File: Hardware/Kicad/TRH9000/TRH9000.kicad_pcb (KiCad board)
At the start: 2 copper layers, 99.1 x 63.5 mm, 63 parts, among them J1 RGB, J100 MSX_SLOT_CONNECTOR, J2 S-Video, J3 Composite, Q1 BC817, U1 V9990, U2 KM428C256, U3 KM428C256, U4 74HC138, U5 74HC32, U6 CXA2075M, X1 14.318Mhz, Y1 21.47727Mhz

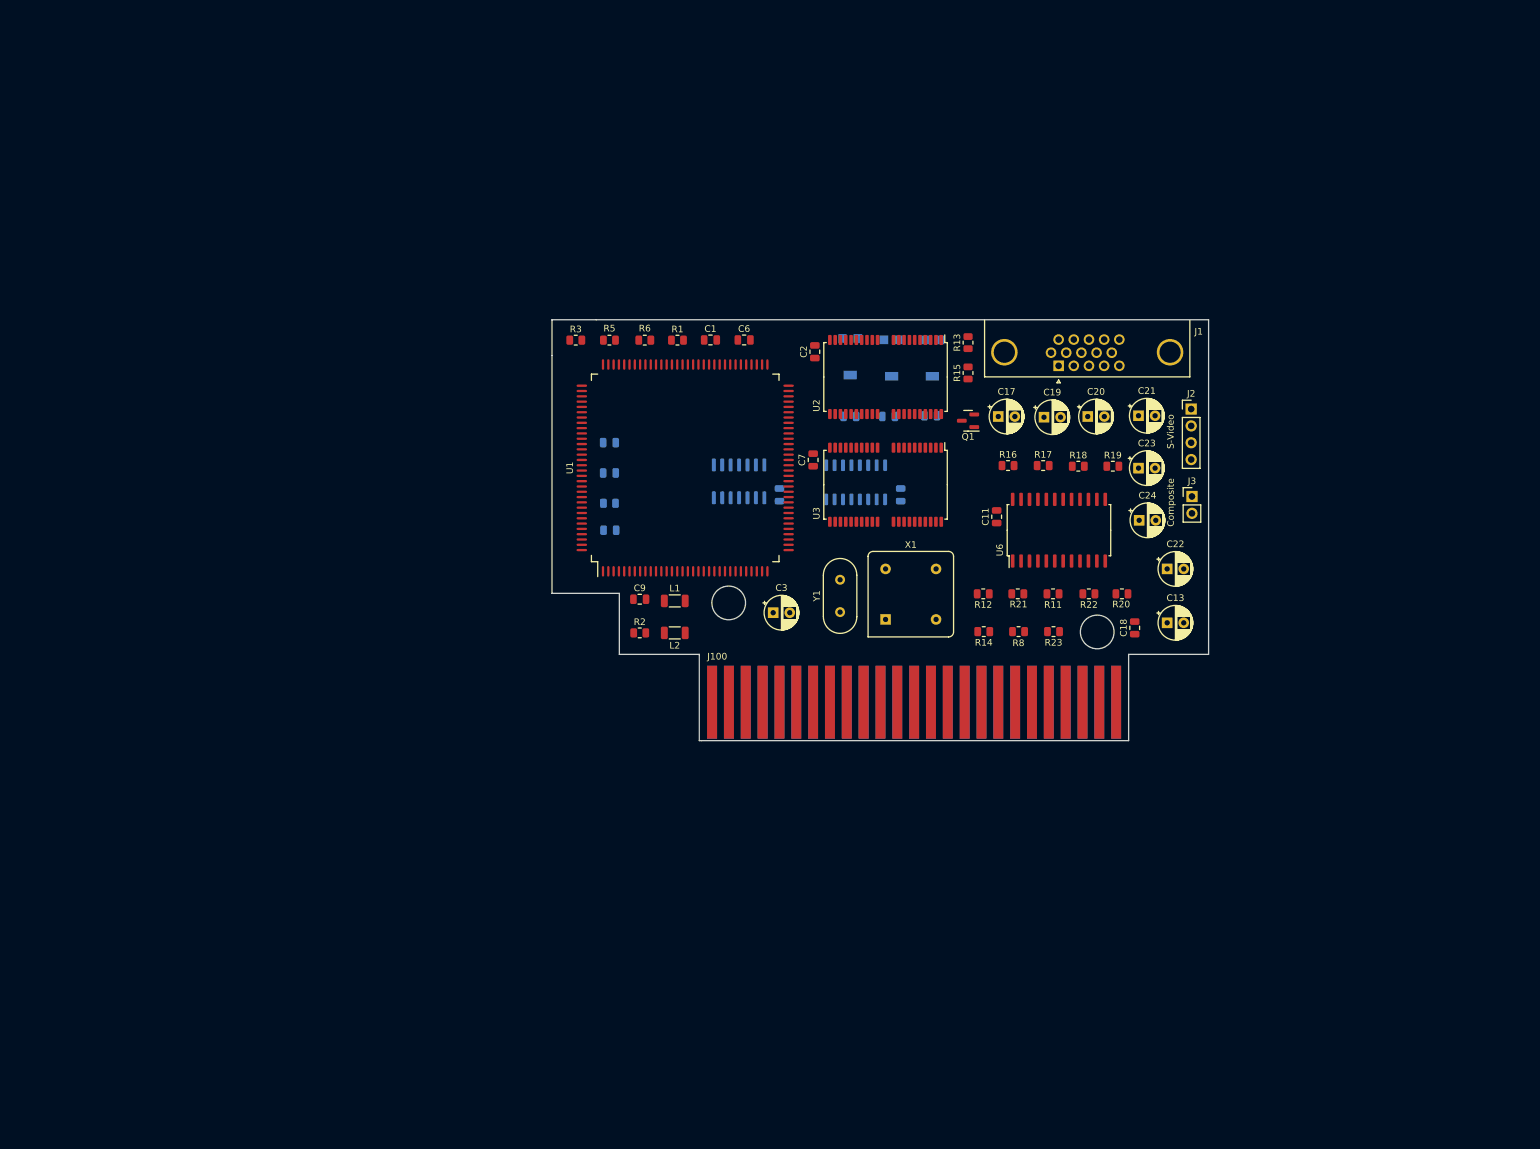
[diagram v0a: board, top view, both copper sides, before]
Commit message: Routing 1. First 3d view of the current PCB.
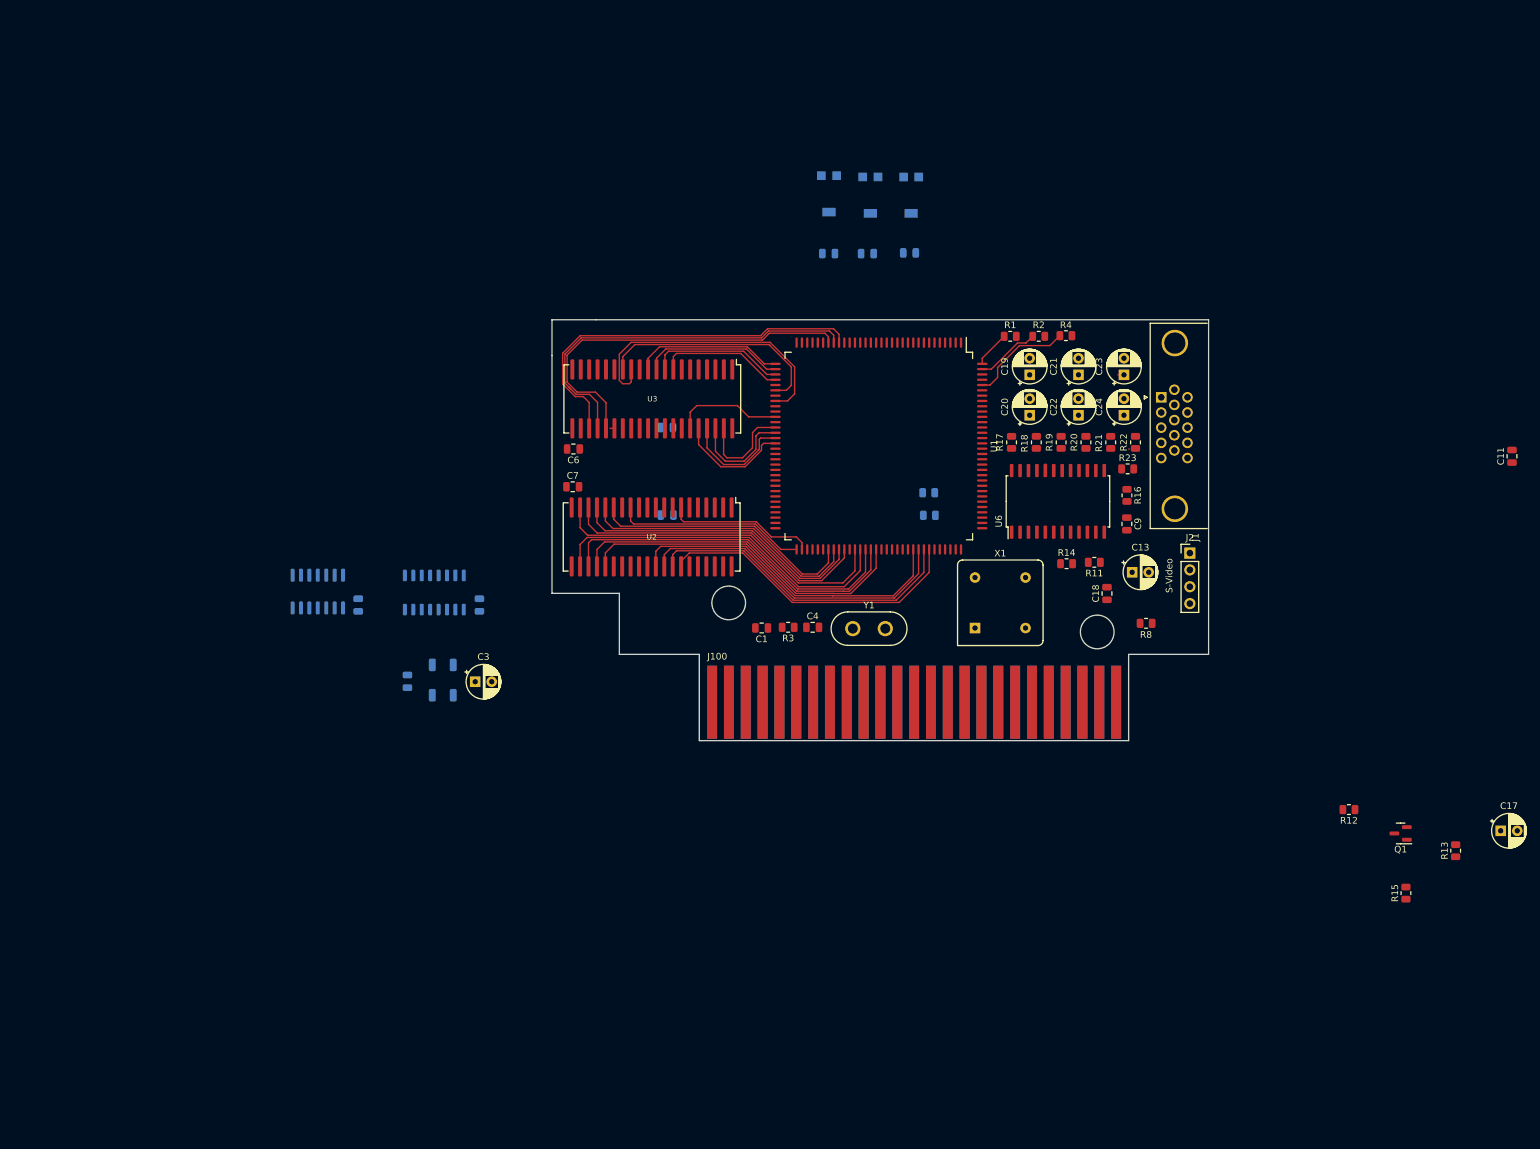
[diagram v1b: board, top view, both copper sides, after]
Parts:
- removed J3: Composite, Connector_PinHeader_2.54mm:PinHeader_1x02_P2.54mm_Vertical
- C2, L1, L2, R5, R6: moved to B.Cu
- C4, R4: moved to F.Cu
- U2, U3: footprint trh9000:TSOP-II-40_10.16x18.41mm_P0.8mm -> trh9000:SOJ-40_400mil
- Y1: footprint Crystal:Crystal_HC49-U_Vertical -> Crystal:Crystal_HC50_Vertical
- moved R13 106.2 mm to (234.6, 143.6)
- moved R15 102.6 mm to (227.1, 150.0)
- moved C17 98.2 mm to (241.4, 140.6)
- moved Q1 90.2 mm to (226.3, 141.0)
- moved C2 79.1 mm to (76.5, 118.0)
- moved C11 78.3 mm to (243.1, 84.1)
- moved R2 75.0 mm to (171.7, 66.0), turned to 180 degrees
- moved C9 74.4 mm to (185.0, 94.3), turned to -90 degrees
- moved R4 73.4 mm to (175.8, 65.9)
- moved C10 65.7 mm to (87.3, 106.5)
- moved U5 65.7 mm to (62.9, 104.5)
- moved C12 65.7 mm to (69.0, 106.5)
- moved U4 65.7 mm to (80.5, 104.6)
- moved R12 64.1 mm to (218.5, 137.4)
- moved R3 53.9 mm to (133.9, 109.9), turned to 180 degrees
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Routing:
- net /VDP/V0A2: track 0.00 -> 58.5 mm
- net /VDP/V0A1: track 0.00 -> 58.1 mm
- net /VDP/V0A0: track 0.00 -> 57.0 mm
- net /VDP/V1A3: track 0.00 -> 53.3 mm
- net /VDP/V1A2: track 0.00 -> 53.1 mm
- net /VDP/V1A4: track 0.00 -> 52.0 mm
- net /VDP/V1A1: track 0.00 -> 51.9 mm
- net /VDP/V1A0: track 0.00 -> 50.9 mm
- net /VDP/V1D4: track 0.00 -> 49.7 mm
- net /VDP/V1D5: track 0.00 -> 48.8 mm
- net /VDP/V1D6: track 0.00 -> 48.2 mm
- net /VDP/V1A5: track 0.00 -> 47.4 mm
- net /VDP/V1D7: track 0.00 -> 47.2 mm
- net /VDP/V1A6: track 0.00 -> 45.0 mm
- net Net-(U1-Pad40): track 0.00 -> 44.1 mm
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
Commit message: Many changes, among them, replacing the Composite out with SCART-rgb.
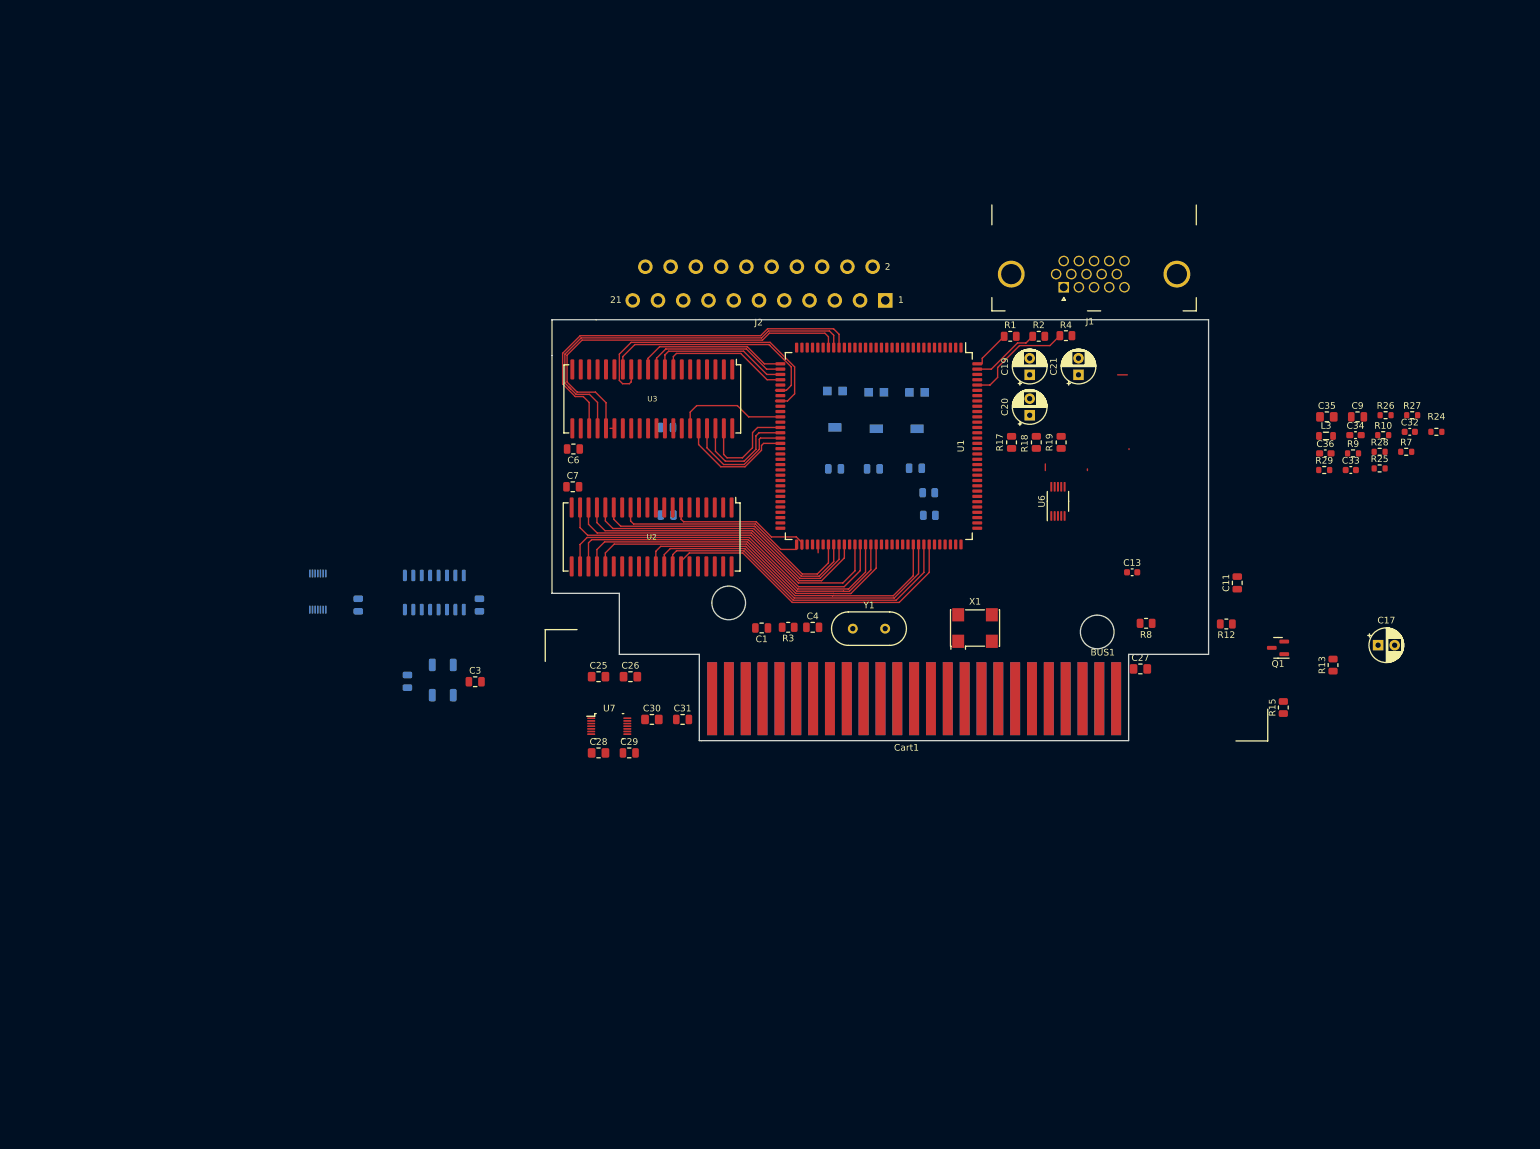
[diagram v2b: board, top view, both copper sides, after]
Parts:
- removed C18: 47pF, Capacitor_SMD:C_0805_2012Metric
- removed C22, C23, C24: 220uF, Capacitor_THT:CP_Radial_D5.0mm_P2.50mm
- removed J100: MSX_SLOT_CONNECTOR, msx:msx_cartridge
- removed R11: 4K7, Resistor_SMD:R_0805_2012Metric
- removed R14: 2K2, Resistor_SMD:R_0805_2012Metric
- removed R16: 2K61, Resistor_SMD:R_0805_2012Metric
- removed R20: 43R, Resistor_SMD:R_0805_2012Metric
- removed R21, R22: 75R, Resistor_SMD:R_0805_2012Metric
- removed R23: 240R, Resistor_SMD:R_0805_2012Metric
- removed REF**: OSHW-Logo_11.4x12mm_SilkScreen, Symbol:OSHW-Logo_11.4x12mm_SilkScreen
- added BUS1: MSX_SLOT_EDGE-CON, trh9000:msx_cartridge, F.Cu at (152.9, 120.8)
- added C25: C_CL21B105KBFNNNF, Capacitor_SMD:C_0805_2012Metric_Pad1.18x1.45mm_HandSolder, F.Cu at (105.3, 117.3)
- added C26: C_CL21B105KBFNNNF, Capacitor_SMD:C_0805_2012Metric_Pad1.18x1.45mm_HandSolder, F.Cu at (110.1, 117.3)
- added C27: C_CL21B105KBFNNNF, Capacitor_SMD:C_0805_2012Metric_Pad1.18x1.45mm_HandSolder, F.Cu at (187.0, 116.2)
- added C28: C_CL21B105KBFNNNF, Capacitor_SMD:C_0805_2012Metric_Pad1.18x1.45mm_HandSolder, F.Cu at (105.3, 128.8)
- added C29: C_CC0805JPX7R9BB104, Capacitor_SMD:C_0805_2012Metric, F.Cu at (109.9, 128.8)
- added C30: C_CL21B105KBFNNNF, Capacitor_SMD:C_0805_2012Metric_Pad1.18x1.45mm_HandSolder, F.Cu at (113.3, 123.8)
- added C31: C_CC0805JPX7R9BB104, Capacitor_SMD:C_0805_2012Metric, F.Cu at (118.0, 123.8)
- added C32: 47pF, Capacitor_SMD:C_0603_1608Metric, F.Cu at (227.7, 80.4)
- added C33: 47pF, Capacitor_SMD:C_0603_1608Metric, F.Cu at (218.8, 86.2)
- added C34: C_CL10B104KB8NNNL, Capacitor_SMD:C_0603_1608Metric_Pad1.08x0.95mm_HandSolder, F.Cu at (219.5, 80.9)
- added C35: C_GRM21BR71A106KA73K, Capacitor_SMD:C_0805_2012Metric_Pad1.18x1.45mm_HandSolder, F.Cu at (215.2, 78.2)
- added C36: C_CL10B104KB8NNNL, Capacitor_SMD:C_0603_1608Metric_Pad1.08x0.95mm_HandSolder, F.Cu at (214.9, 83.7)
- added Cart1: MSX-cartridge_dummy, trh9000:MSX-cart-dummy, F.Cu at (151.8, 118.7)
- added L3: L_MLZ2012M4R7HT000, Inductor_SMD:L_0805_2012Metric, F.Cu at (215.0, 81.0)
- added R10: 100, Resistor_SMD:R_0603_1608Metric, F.Cu at (223.7, 80.9)
- added R24: R_RC0603FR-0710KL, LRJ:R_0603_1608Metric_roundcourt, F.Cu at (231.7, 80.4)
- added R25: 100, Resistor_SMD:R_0603_1608Metric, F.Cu at (223.1, 85.9)
- added R26: 100, Resistor_SMD:R_0603_1608Metric, F.Cu at (224.0, 77.9)
- added R27: 100, Resistor_SMD:R_0603_1608Metric, F.Cu at (228.0, 77.9)
- added R28: 100, Resistor_SMD:R_0603_1608Metric, F.Cu at (223.1, 83.4)
- added R29: 1k, Resistor_SMD:R_0603_1608Metric, F.Cu at (214.8, 86.2)
- added R7: R_ERJ-3GEYJ105V, Resistor_SMD:R_0603_1608Metric, F.Cu at (227.1, 83.4)
- added R9: 75, Resistor_SMD:R_0603_1608Metric, F.Cu at (219.1, 83.7)
- added U7: T.I_SN74AHCT32D, trh9000:Texas_R-PDSO-G14_3.6x4.4mm, F.Cu at (106.9, 124.8)
- C10, C11, C12, C5, C7: value 100nF -> C_CC0805JPX7R9BB104
- C13: value 47pF -> C_GRM188D71A106KA73D; footprint Capacitor_THT:CP_Radial_D5.0mm_P2.50mm -> Capacitor_SMD:C_0603_1608Metric
- C3: value 47uF -> C_GRM21BR61A476ME15K; footprint Capacitor_THT:CP_Radial_D5.0mm_P2.50mm -> Capacitor_SMD:C_0805_2012Metric
- C6, C8: value 100nF -> 10nF
- C9: value 100nF -> 47pF
- J1: footprint Connector_Dsub:DSUB-15-HD_Female_Horizontal_P2.29x1.98mm_EdgePinOffset3.03mm_Housed_MountingHolesOffset4.94mm -> LRJ:DSUB-Amphenol_L77HDE15SD1CH4RHNVGA
- J2: value S-Video -> Console5_SCART; footprint Connector_PinHeader_2.54mm:PinHeader_1x04_P2.54mm_Vertical -> LRJ:SCART-21_Female_Horizontal_P1.905x2.54mm_EdgePinOffset10.7mm
- U1: footprint trh9000:QFP-128_28x28_Pitch0.8mm -> trh9000:LQFP-128_28x28mm_P0.8mm
- U4: value 74HC138 -> 74VHC138
- U5: value 74HC32 -> T.I_SN74AHCT32D; footprint Package_SO:SO-14_3.9x8.65mm_P1.27mm -> trh9000:Texas_R-PDSO-G14_3.6x4.4mm
- U6: value CXA2075M -> LMH1980; footprint Package_SO:SOP-24_7.5x15.4mm_P1.27mm -> Package_SO:VSSOP-10_3x3mm_P0.5mm
- X1: value 14.318Mhz -> Crystek_CE3291; footprint Oscillator:Oscillator_DIP-8 -> Oscillator:Oscillator_SMD_Abracon_ASV-4Pin_7.0x5.1mm
- Y1: footprint Crystal:Crystal_HC50_Vertical -> Crystal:Crystal_HC49-U_Vertical
- moved J2 84.4 mm to (129.5, 44.8)
- moved C11 45.6 mm to (201.7, 103.2)
- moved C9 38.4 mm to (219.8, 78.2), turned to 0 degrees
- moved C17 33.6 mm to (222.9, 112.6)
- moved Q1 33.6 mm to (207.8, 113.0)
- moved R12 33.6 mm to (200.0, 109.4)
- moved R13 33.6 mm to (216.1, 115.6)
- moved R15 33.6 mm to (208.6, 122.0)
- moved C16 32.5 mm to (153.1, 85.9)
- moved RV3 32.5 mm to (153.3, 77.2)
- moved C14 32.5 mm to (140.9, 86.0)
- moved C15 32.5 mm to (146.8, 86.0)
- moved RV1 32.5 mm to (140.9, 77.0)
- moved RV2 32.5 mm to (147.2, 77.2)
- moved J1 26.2 mm to (180.1, 51.0), turned to 180 degrees
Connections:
- net /CLK renamed /SYS_CLK
- net /VIDEO/SCIN renamed /SCIN
- net /~{/INT} renamed /~{INT}
- net /~{/WAIT} renamed /~{WAIT}
- net Net-(C1-Pad1) renamed /VDP/X1
- net Net-(C14-Pad2) renamed /VIDEO/RIN
- net Net-(C15-Pad2) renamed /VIDEO/GIN
- net Net-(C16-Pad2) renamed /VIDEO/BIN
- net Net-(C4-Pad1) renamed /VDP/X2
- net Net-(R4-Pad2) renamed /VDP/VMREQ
- net Net-(U1-Pad38) renamed /VDP/~{V0_RAS}
- net Net-(U1-Pad39) renamed /VDP/~{V0_CAS}
- net Net-(U1-Pad40) renamed /VDP/~{V0_WE}
- net Net-(U1-Pad41) renamed /VDP/~{V0_TR}
- net Net-(U1-Pad42) renamed /VDP/~{V0_SC}
- net Net-(U1-Pad43) renamed /VDP/~{VO_SOE}
- net Net-(U1-Pad62) renamed /VDP/~{V1_RAS}
- net Net-(U1-Pad63) renamed /VDP/~{V1_CAS}
- net Net-(U1-Pad65) renamed /VDP/~{V1_WE}
- net Net-(U1-Pad66) renamed /VDP/~{V1_TR}
- net Net-(U1-Pad67) renamed /VDP/~{V1_SC}
- net Net-(U1-Pad68) renamed /VDP/~{V1_SOE}
- C11 pad 1: +5V -> GND
- C11 pad 2: GND -> +12V
- C12 pad 1: +5V -> -12V
- C13 pad 1: Net-(C13-Pad1) -> GND
- C13 pad 2: GND -> GND1
- C14 pad 1: Net-(C14-Pad1) -> /VIDEO/RO
- C15 pad 1: Net-(C15-Pad1) -> /VIDEO/GO
- C16 pad 1: Net-(C16-Pad1) -> /VIDEO/BO
- C8 pad 1: +5V -> GND
- C8 pad 2: GND -> +5V
- C9 pad 1: +5V -> Net-(C9-Pad1)
- J1 pad 10: GND -> GND1
- J1 pad 13: /VIDEO/SYNCOUT -> /VIDEO/HSYNC
- J1 pad 14: unconnected-(J1-Pad14) -> /VIDEO/VSYNC
- J1 pad 5: GND -> GND1
- J1 pad 6: GND -> GNDA
- J1 pad 7: GND -> GNDA
- J1 pad 8: GND -> GNDA
- J2 pad 1: GND -> unconnected-(J2-Pad1)
- J2 pad 2: GND -> unconnected-(J2-Pad2)
- J2 pad 3: /VIDEO/YOUT -> unconnected-(J2-Pad3)
- J2 pad 4: /VIDEO/COUT -> GNDA
- L1 pad 1: GND -> +5V
- L1 pad 2: GNDA -> +5VA
- L2 pad 1: +5V -> GND
- L2 pad 2: +5VA -> GNDA
- R15 pad 1: /VIDEO/SYNCOUT -> /VIDEO/CSYNCO
- R17 pad 2: Net-(R17-Pad2) -> /VIDEO/RO
- R18 pad 2: Net-(R18-Pad2) -> /VIDEO/GO
- R19 pad 2: Net-(R19-Pad2) -> /VIDEO/BO
- R5 pad 2: Net-(R5-Pad2) -> /VDP/HRESET
- R6 pad 1: +5V -> /VDP/VRESET
- R6 pad 2: Net-(R6-Pad2) -> +5V
- R8 pad 1: Net-(C13-Pad1) -> Net-(C9-Pad1)
- U1 pad 105: Net-(R6-Pad2) -> /VDP/HRESET
- U1 pad 106: Net-(R5-Pad2) -> /VDP/VRESET
- U1 pad 113: Net-(U1-Pad113) -> /VDP/MCKIN
- U1 pad 2: /VDP/~{VDPW} -> /VDP/~{VDPR}
- U1 pad 3: /VDP/~{VDPR} -> /VDP/~{VDPW}
- U4 pad 4: /~{/IORQ} -> /~{IORQ}
- U4 pad 6: /~{/M1} -> /~{M1}
- U5 pad 1: /~{/RD} -> /~{RD}
- U5 pad 14: +5V -> (no net)
- U5 pad 4: /~{/WR} -> /~{WR}
- U5 pad 7: GND -> (no net)
- U6 pad 1: GND -> Net-(R24-Pad2)
- U6 pad 10: Net-(C18-Pad1) -> unconnected-(U6-Pad10)
- U6 pad 2: Net-(C14-Pad1) -> GND
- U6 pad 3: Net-(C15-Pad1) -> +5VA
- U6 pad 4: Net-(C16-Pad1) -> /VIDEO/SYNCIN
- U6 pad 6: Net-(C13-Pad1) -> Net-(R25-Pad2)
- X1 pad 4: GND -> +5V
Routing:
- net Net-(C23-Pad1): track 1.46 -> 0.00 mm
- net GNDA: track 0.00 -> 1.46 mm
- net (no net): track 0.00 -> 1.38 mm
- net Net-(R20-Pad2): track 1.00 -> 0.00 mm
